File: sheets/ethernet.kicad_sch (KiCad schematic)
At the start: 44 parts, among them J8 2250504-1, Q36 2N7002, Q37 2N7002, Q38 2N7002, U11 93C46, U12 AP2112K-1.0, U9 RTL8125BG-CG, Y2 25MHz

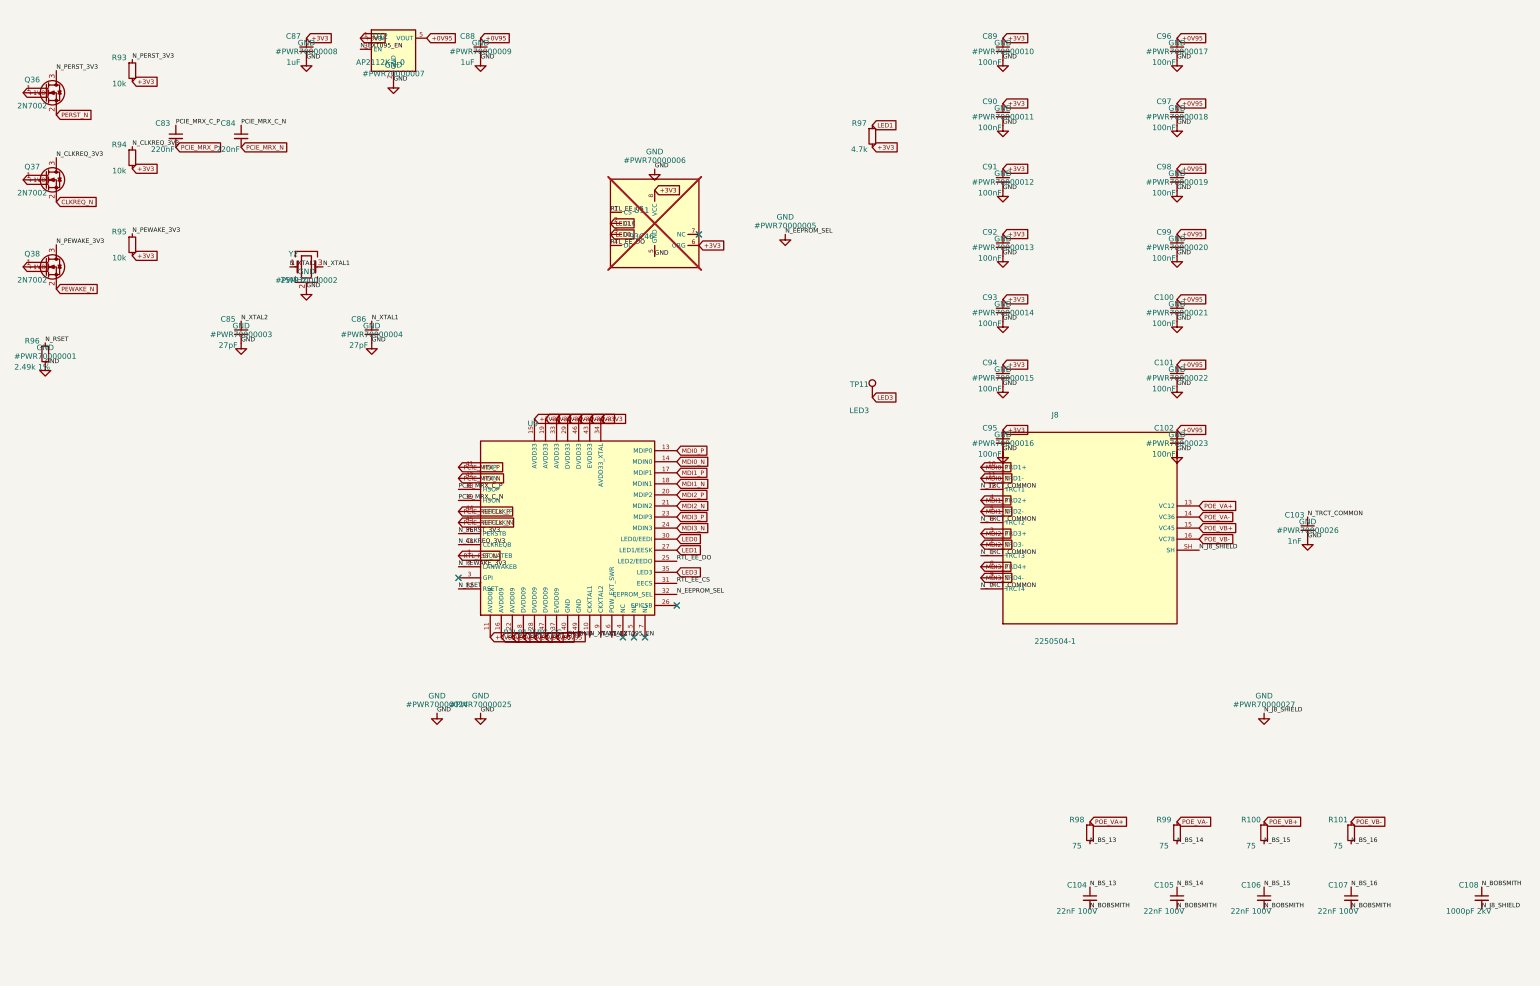
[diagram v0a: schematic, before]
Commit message: sch: ethernet rework — core supply per variant decision, MDI0 polarity, reference alignment, dedicated 1MHz+ 3V3_ETH
Co-Authored-By: Claude Fable 5 <noreply@anthropic.com>
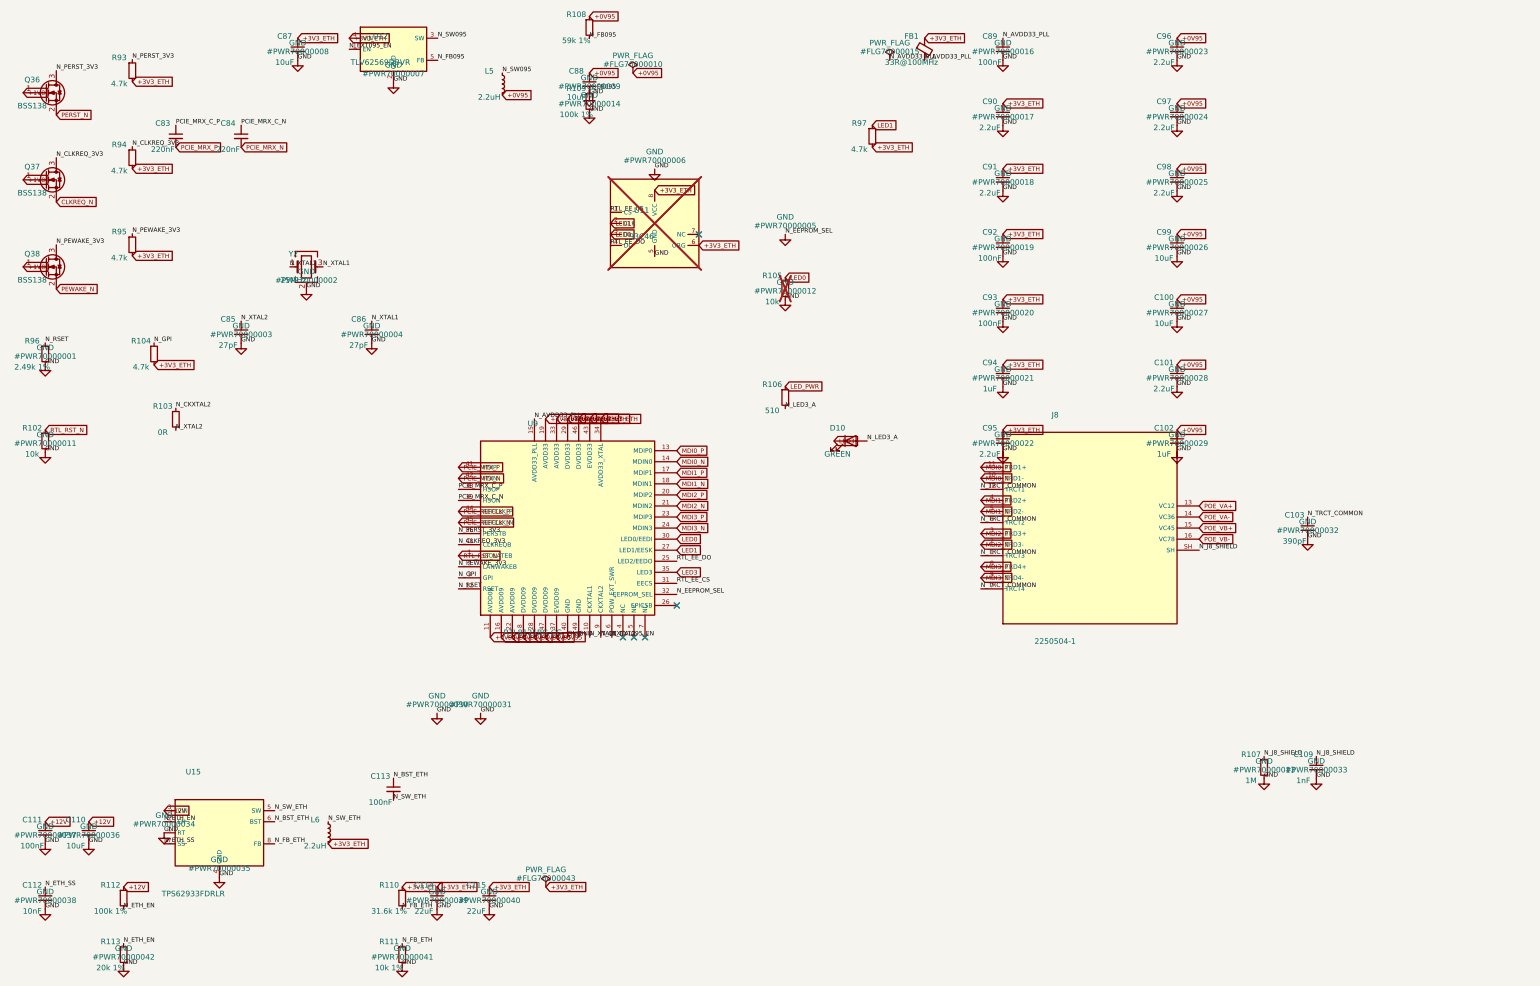
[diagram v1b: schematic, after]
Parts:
- removed C104, C105, C106, C107: 22nF 100V, Capacitor_SMD:C_0603_1608Metric, symbol Device:C_Small
- removed C108: 1000pF 2kV, Capacitor_SMD:C_0603_1608Metric, symbol Device:C_Small
- removed Q36, Q37, Q38: 2N7002, Package_TO_SOT_SMD:SOT-23, symbol Transistor_FET:2N7002
- removed R100, R101, R98, R99: 75, Resistor_SMD:R_0603_1608Metric, symbol Device:R_Small
- removed TP11: LED3, TestPoint:TestPoint_Pad_D1.5mm, symbol Connector:TestPoint
- removed U12: AP2112K-1.0, Package_TO_SOT_SMD:SOT-23-5, symbol sierra-to-usb:AP2112K-1.0
- added C109: 1nF, Capacitor_SMD:C_0603_1608Metric, symbol Device:C_Small
- added C110: 10uF, Capacitor_SMD:C_0603_1608Metric, symbol Device:C_Small
- added C111, C113: 100nF, Capacitor_SMD:C_0402_1005Metric, symbol Device:C_Small
- added C112: 10nF, Capacitor_SMD:C_0603_1608Metric, symbol Device:C_Small
- added C114, C115: 22uF, Capacitor_SMD:C_0805_2012Metric, symbol Device:C_Small
- added D10: GREEN, LED_SMD:LED_0603_1608Metric, symbol Device:LED
- added FB1: 33R@100MHz, Inductor_SMD:L_0603_1608Metric, symbol Device:FerriteBead_Small
- added L5, L6: 2.2uH, Inductor_SMD:L_1210_3225Metric, symbol Device:L_Small
- added Q36, Q37, Q38: BSS138, Package_TO_SOT_SMD:SOT-23, symbol Transistor_FET:BSS138
- added R102, R105: 10k, Resistor_SMD:R_0603_1608Metric, symbol Device:R_Small
- added R103: 0R, Resistor_SMD:R_0603_1608Metric, symbol Device:R_Small
- added R104: 4.7k, Resistor_SMD:R_0603_1608Metric, symbol Device:R_Small
- added R106: 510, Resistor_SMD:R_0603_1608Metric, symbol Device:R_Small
- added R107: 1M, Resistor_SMD:R_0603_1608Metric, symbol Device:R_Small
- added R108: 59k 1%, Resistor_SMD:R_0603_1608Metric, symbol Device:R_Small
- added R109, R112: 100k 1%, Resistor_SMD:R_0603_1608Metric, symbol Device:R_Small
- added R110: 31.6k 1%, Resistor_SMD:R_0603_1608Metric, symbol Device:R_Small
- added R111: 10k 1%, Resistor_SMD:R_0603_1608Metric, symbol Device:R_Small
- added R113: 20k 1%, Resistor_SMD:R_0603_1608Metric, symbol Device:R_Small
- added U12: TLV62569DBVR, Package_TO_SOT_SMD:SOT-23-5, symbol sierra-to-usb:TLV62569
- added U15: TPS62933FDRLR, Package_TO_SOT_SMD:SOT-583-8, symbol sierra-to-usb:TPS62933F
- C100, C99: value 100nF -> 10uF; footprint Capacitor_SMD:C_0402_1005Metric -> Capacitor_SMD:C_0603_1608Metric
- C101, C90, C91, C95, C96, C97, C98: value 100nF -> 2.2uF; footprint Capacitor_SMD:C_0402_1005Metric -> Capacitor_SMD:C_0603_1608Metric
- C102, C94: value 100nF -> 1uF; footprint Capacitor_SMD:C_0402_1005Metric -> Capacitor_SMD:C_0603_1608Metric
- C103: value 1nF -> 390pF
- C87, C88: value 1uF -> 10uF
- R93, R94, R95: value 10k -> 4.7k
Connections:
- net +0V95: now also L5.2, R108.1
- net +1V8: now also Q36.1 (G), Q37.1 (G), Q38.1 (G)
- net CLKREQ_N: now also Q37.2 (S)
- net GND: now also C109.2, C110.2, C111.2, C112.2, C114.2, C115.2, R102.2, R105.2, R107.2, R109.2, R111.2, R113.2, U12.2 (GND), U15.1 (RT), U15.4 (GND); no longer J8.SH
- net LED0: now also R105.1
- net LED3: now also D10.1 (K)
- net MDI0_N: now also J8.10 (TRD1-); no longer J8.11 (TRD1-)
- net MDI0_P: now also J8.11 (TRD1+); no longer J8.10 (TRD1+)
- net N_CLKREQ_3V3: now also Q37.3 (D)
- net N_EXT095_EN: now also U12.1 (EN)
- net N_PERST_3V3: now also Q36.3 (D)
- net N_PEWAKE_3V3: now also Q38.3 (D)
- net N_XTAL2: now also R103.2; no longer U9.9 (CKXTAL2)
- net PERST_N: now also Q36.2 (S)
- net PEWAKE_N: now also Q38.2 (S)
- net RTL_RST_N: now also R102.1
- net N_GPI: now reaches U9.3 (GPI)
- net N_GPI: now also R104.1
- net +3V3 renamed +3V3_ETH
- net +3V3_ETH: now also C114.1, C115.1, FB1.1, L6.2, R104.2, R110.1, U12.4 (VIN); no longer C89.1, U9.15 (AVDD33)
- new net +12V: C110.1, C111.1, R112.1, U15.3 (VIN)
- new net LED_PWR: R106.1
- new net N_AVDD33_PLL: C89.1, FB1.2, U9.15 (AVDD33_PLL)
- new net N_BST_ETH: C113.1, U15.6 (BST)
- new net N_CKXTAL2: R103.1, U9.9 (CKXTAL2)
- new net N_ETH_EN: R112.2, R113.1, U15.2 (EN)
- new net N_ETH_SS: C112.1, U15.7 (SS)
- new net N_FB095: R108.2, R109.1, U12.5 (FB)
- new net N_FB_ETH: R110.2, R111.1, U15.8 (FB)
- new net N_J8_SHIELD: C109.1, J8.SH, R107.1
- new net N_LED3_A: D10.2 (A), R106.2
- new net N_SW095: L5.1, U12.3 (SW)
- new net N_SW_ETH: C113.2, L6.1, U15.5 (SW)
- no-connect marks 6 -> 5

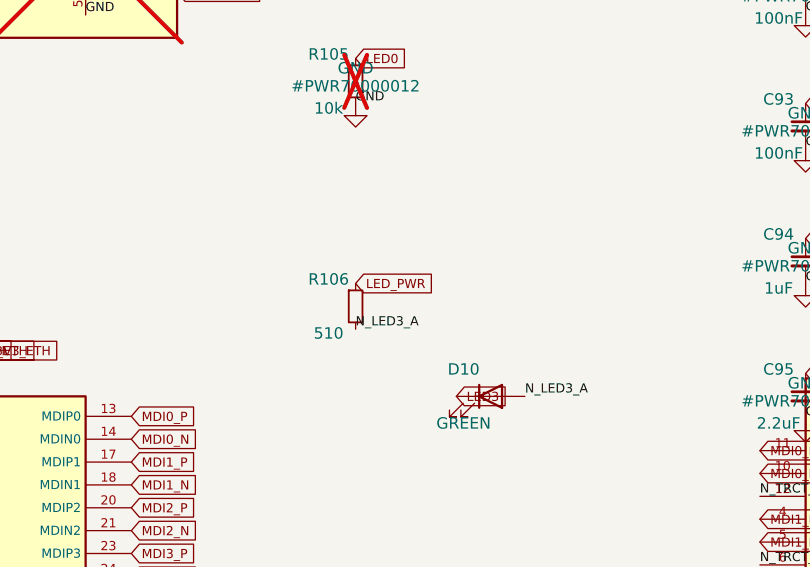
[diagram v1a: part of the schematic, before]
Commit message: sch: ethernet — link LED on +3V3_ETH (spec kill-rail clause + back-feed corner)
Co-Authored-By: Claude Fable 5 <noreply@anthropic.com>
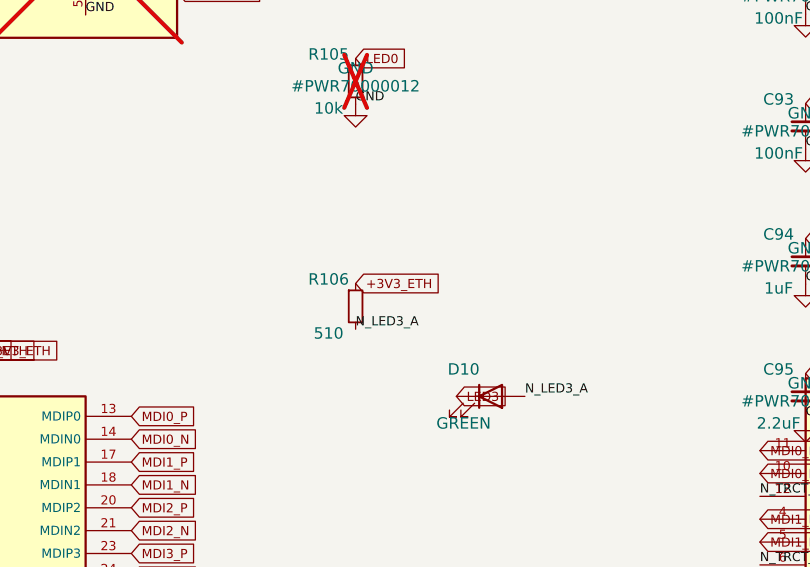
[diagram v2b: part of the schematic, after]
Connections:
- net LED_PWR is gone; now on net +3V3_ETH: R106.1
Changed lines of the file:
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@@
 		(effects (font (size 1.016 1.016)) (justify left bottom))
 	)
-	(global_label "LED_PWR"
+	(global_label "+3V3_ETH"
 		(shape input)
 		(at 200 97.46 0)

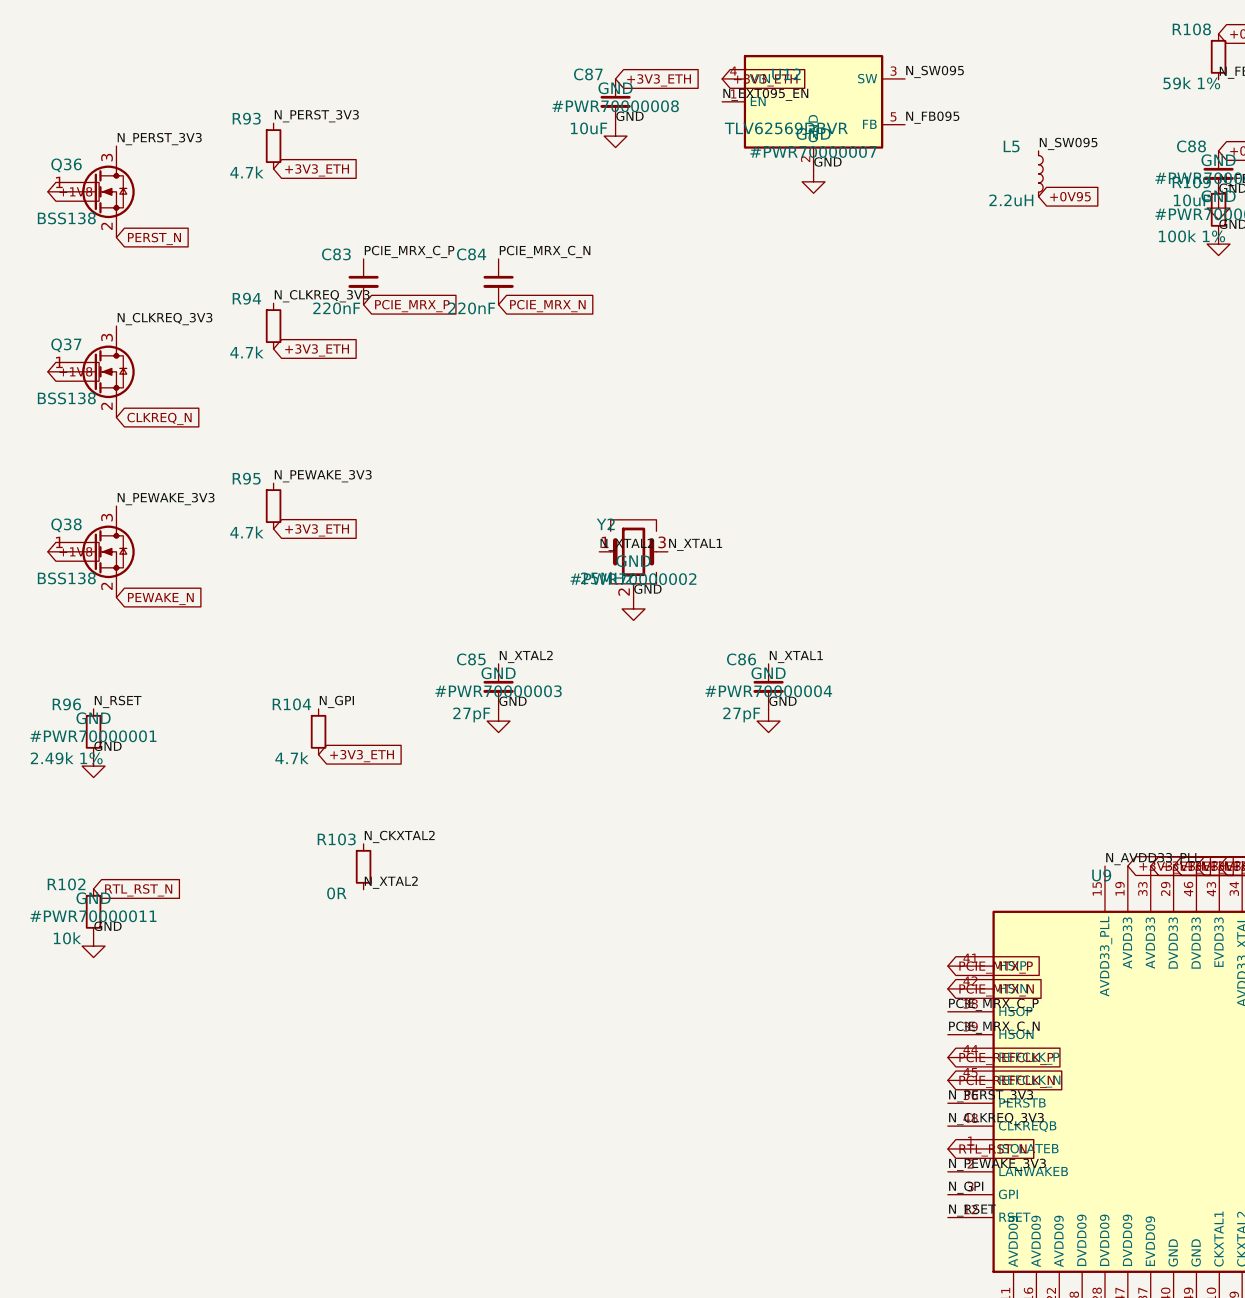
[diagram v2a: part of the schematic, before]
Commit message: sch: audit fixes — buck EN divider corners, 3V3-domain senses, spec §10 LEDs
F1 (critical): TPS565201 BUCK_EN divider (R40/R41) redesigned against the
datasheet's VENH/VENL/REN corners so the 3.3V buck actually starts once the
12V node is negotiated, without false-starting on pre-negotiation 5V VBUS.

F2 (medium): GP18/GP19 retargeted from the RP2040 sheet to the ethernet
sheet's existing 3.3V-domain PERST/CLKREQ shifter outputs; GP17 gets a new
BSS138 level-shift stage (Q40/R122) on m2, mirroring the Task 10 pattern.

F3 (minor): added the two spec §10 indicator LEDs (D29 12V/power, D30
PD-good) that were dropped during Task 4 and never restored.

check_nets.py all pass; ERC 0 errors / 800 warnings (was 788, full delta
accounted in docs/erc-waivers.md); netlist exports clean, no annotation
warnings.

Co-Authored-By: Claude Fable 5 <noreply@anthropic.com>
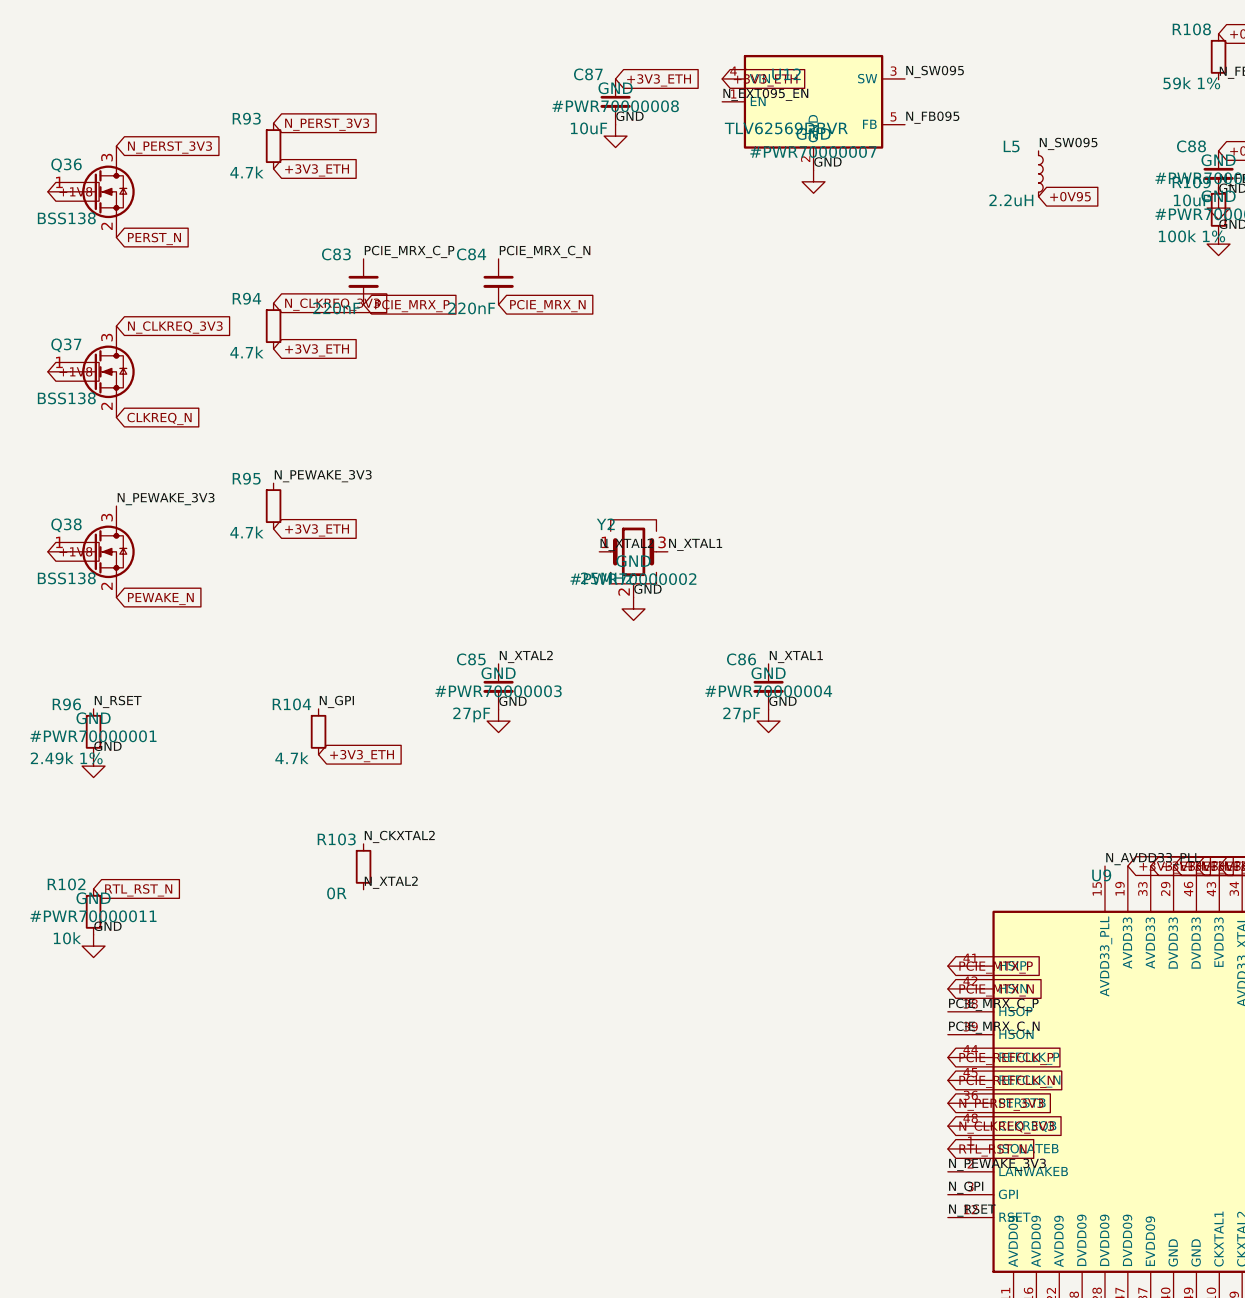
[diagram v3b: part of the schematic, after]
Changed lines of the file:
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@@
 		(property "Intersheetrefs" "${INTERSHEET_REFS}" (at 32.54 35.08 0) (effects (font (size 1.27 1.27))))
 	)
-	(label "N_PERST_3V3"
+	(global_label "N_PERST_3V3"
+		(shape input)
 		(at 32.54 24.92 0)
 		(effects (font (size 1.016 1.016)) (justify left bottom))
+		(property "Intersheetrefs" "${INTERSHEET_REFS}" (at 32.54 24.92 0) (effects (font (size 1.27 1.27))))
 	)
-	(label "N_PERST_3V3"
+	(global_label "N_PERST_3V3"
+		(shape input)
 		(at 50 22.38 0)
 		(effects (font (size 1.016 1.016)) (justify left bottom))
+		(property "Intersheetrefs" "${INTERSHEET_REFS}" (at 50 22.38 0) (effects (font (size 1.27 1.27))))
 	)
 	(global_label "+3V3_ETH"
@@
 		(property "Intersheetrefs" "${INTERSHEET_REFS}" (at 32.54 55.08 0) (effects (font (size 1.27 1.27))))
 	)
-	(label "N_CLKREQ_3V3"
+	(global_label "N_CLKREQ_3V3"
+		(shape input)
 		(at 32.54 44.92 0)
 		(effects (font (size 1.016 1.016)) (justify left bottom))
+		(property "Intersheetrefs" "${INTERSHEET_REFS}" (at 32.54 44.92 0) (effects (font (size 1.27 1.27))))
 	)
-	(label "N_CLKREQ_3V3"
+	(global_label "N_CLKREQ_3V3"
+		(shape input)
 		(at 50 42.38 0)
 		(effects (font (size 1.016 1.016)) (justify left bottom))
+		(property "Intersheetrefs" "${INTERSHEET_REFS}" (at 50 42.38 0) (effects (font (size 1.27 1.27))))
 	)
 	(global_label "+3V3_ETH"
@@
 		(property "Intersheetrefs" "${INTERSHEET_REFS}" (at 50 67.46 0) (effects (font (size 1.27 1.27))))
 	)
-	(label "N_PERST_3V3"
+	(global_label "N_PERST_3V3"
+		(shape input)
 		(at 124.92 131.27 0)
 		(effects (font (size 1.016 1.016)) (justify left bottom))
+		(property "Intersheetrefs" "${INTERSHEET_REFS}" (at 124.92 131.27 0) (effects (font (size 1.27 1.27))))
 	)
-	(label "N_CLKREQ_3V3"
+	(global_label "N_CLKREQ_3V3"
+		(shape input)
 		(at 124.92 133.81 0)
 		(effects (font (size 1.016 1.016)) (justify left bottom))
+		(property "Intersheetrefs" "${INTERSHEET_REFS}" (at 124.92 133.81 0) (effects (font (size 1.27 1.27))))
 	)
 	(label "N_PEWAKE_3V3"
